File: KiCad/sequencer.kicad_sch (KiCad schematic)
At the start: 35 parts, among them J1 GATE OUT, J2 CLOCK IN, J5 RESET, J6 CV OUT, J7 CLOCK OUT, Q1 BC548, SW10 SW_Nidec_CAS-120A1, U1 TL074

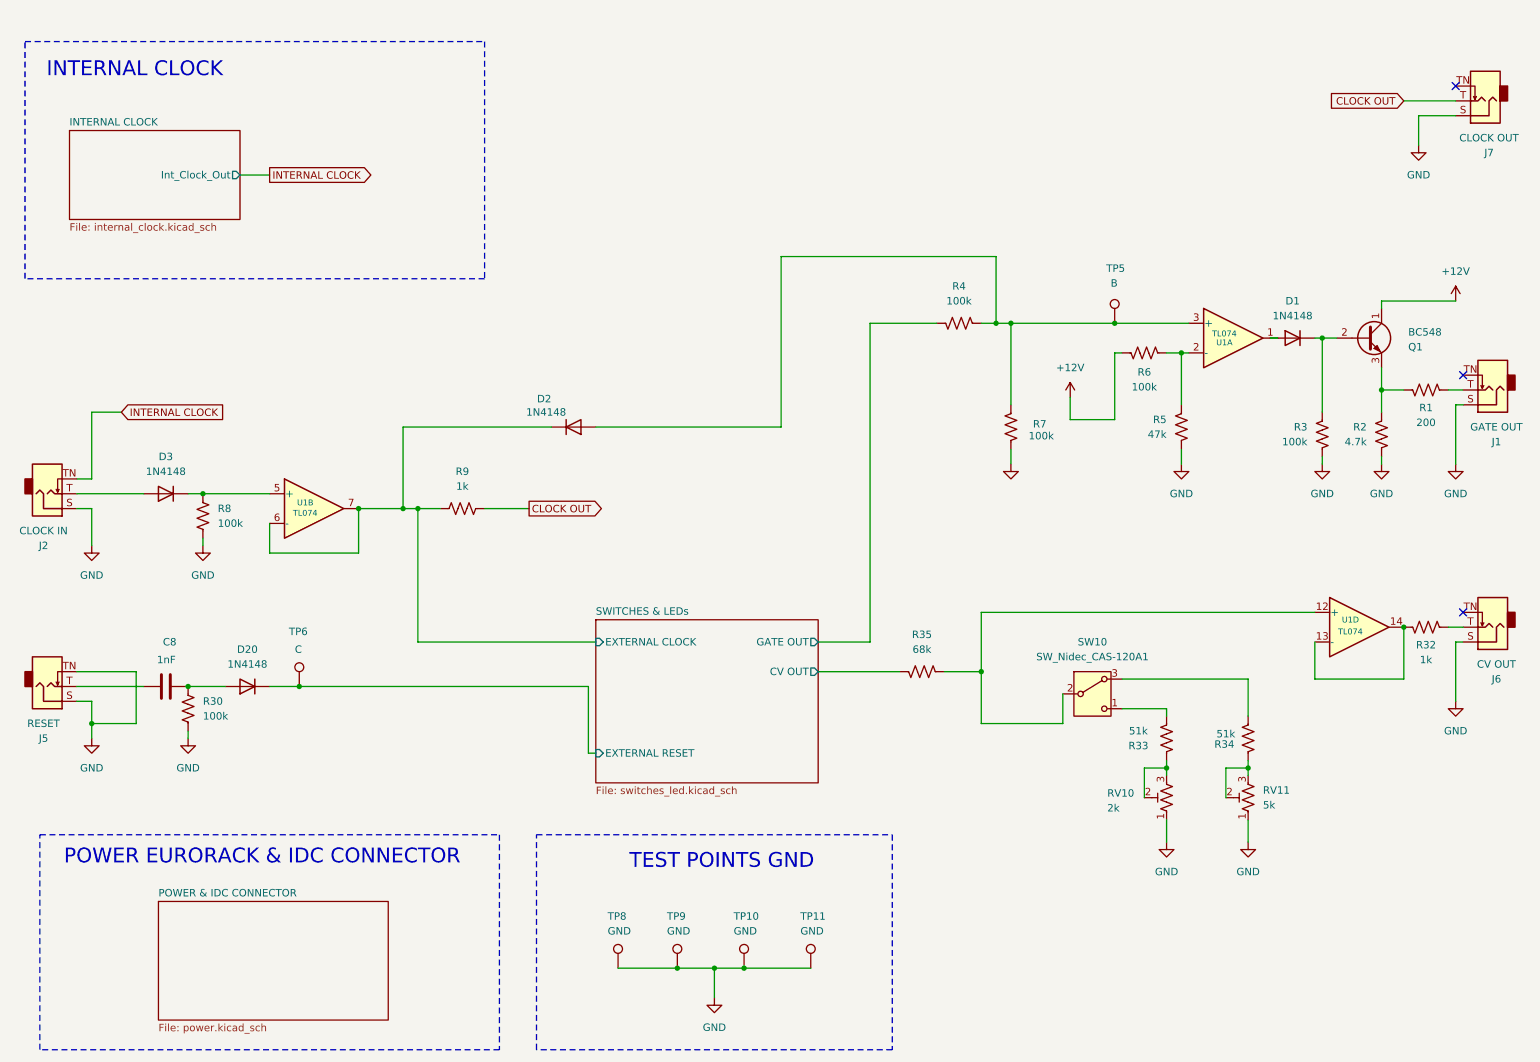
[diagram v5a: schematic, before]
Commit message: Updating sheet names
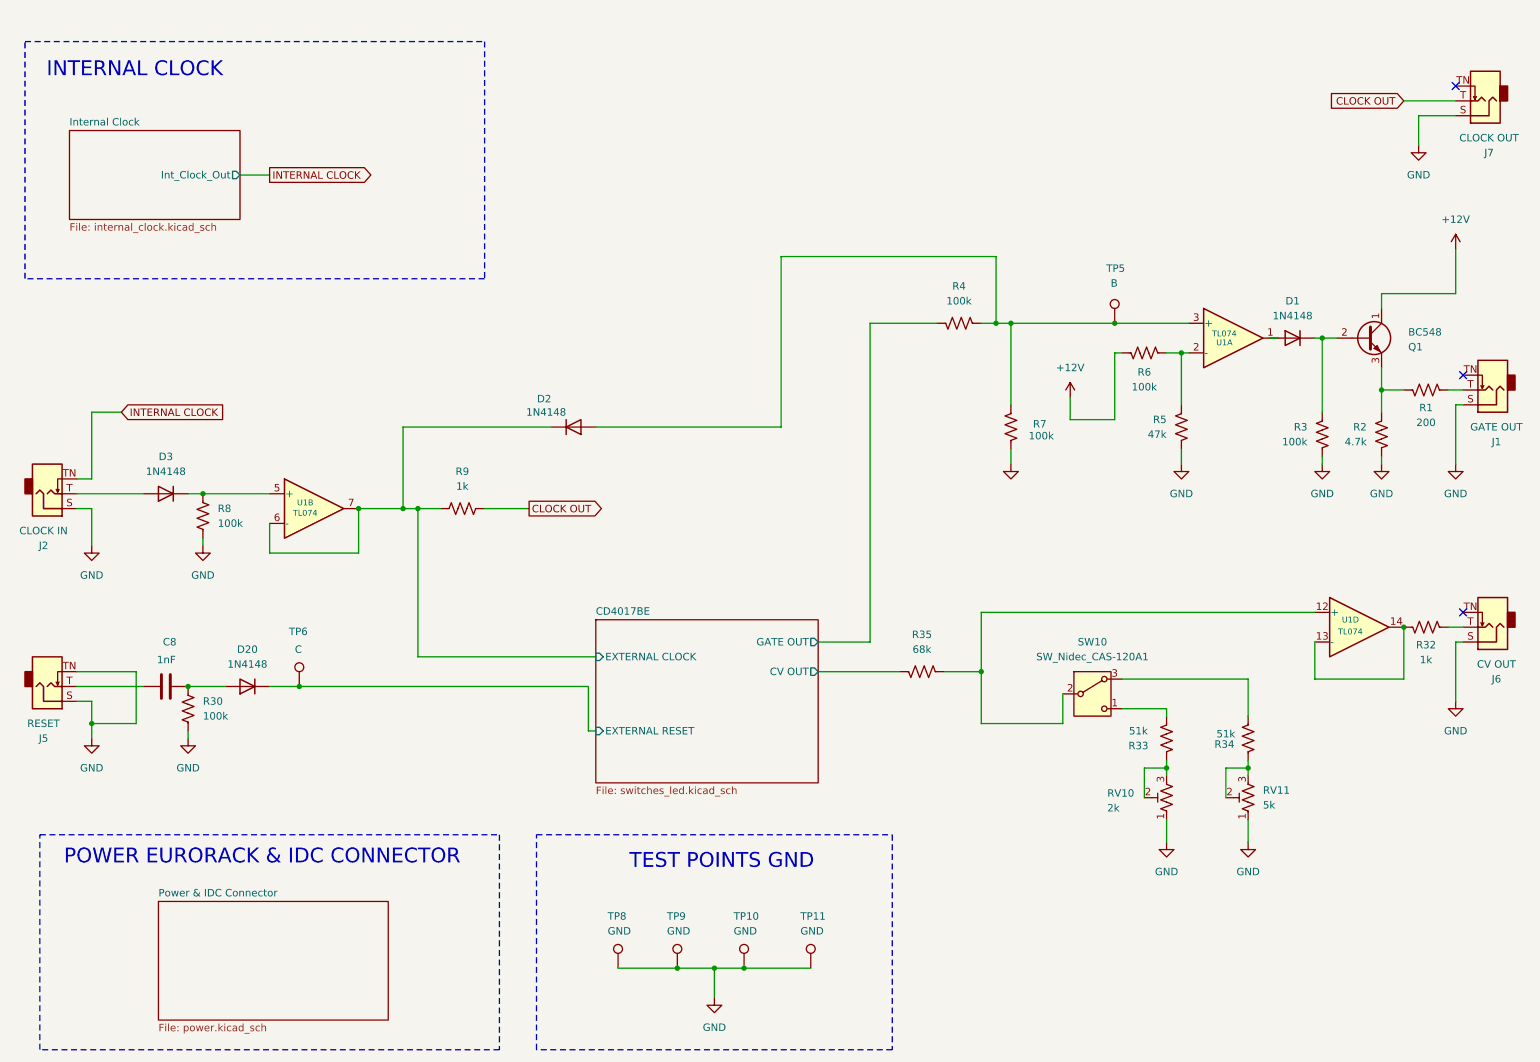
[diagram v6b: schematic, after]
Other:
- sheet INTERNAL CLOCK renamed Internal Clock
- sheet POWER & IDC CONNECTOR renamed Power & IDC Connector
- sheet SWITCHES & LEDs renamed CD4017BE
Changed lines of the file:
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@@
 	(title_block
 		(title "8 Step Sequencer")
-		(date "2026-03-09")
+		(date "2026-03-13")
 		(rev "v0.0")
 		(company "Dirty Dream - Nathanael Noir")
@@
 	(wire
 		(pts
-			(xy 116.84 142.24) (xy 116.84 130.81)
+			(xy 116.84 138.43) (xy 116.84 130.81)
 		)
 		(stroke
@@
 	(wire
 		(pts
-			(xy 252.73 64.77) (xy 265.43 64.77)
+			(xy 252.73 63.5) (xy 265.43 63.5)
 		)
 		(stroke
@@
 	(wire
 		(pts
-			(xy 116.84 142.24) (xy 118.11 142.24)
+			(xy 116.84 138.43) (xy 118.11 138.43)
 		)
 		(stroke
@@
 	(wire
 		(pts
-			(xy 252.73 66.04) (xy 252.73 64.77)
+			(xy 252.73 66.04) (xy 252.73 63.5)
 		)
 		(stroke
@@
 	(wire
 		(pts
-			(xy 87.63 100.33) (xy 87.63 123.19)
+			(xy 87.63 100.33) (xy 87.63 125.73)
 		)
 		(stroke
@@
 	(wire
 		(pts
+			(xy 265.43 55.88) (xy 265.43 63.5)
+		)
+		(stroke
+			(width 0)
+			(type default)
+		)
+	)
+	(wire
+		(pts
 			(xy 265.43 133.35) (xy 265.43 123.19)
 		)
@@
 	(wire
 		(pts
-			(xy 87.63 123.19) (xy 118.11 123.19)
+			(xy 87.63 125.73) (xy 118.11 125.73)
 		)
 		(stroke
@@
 	(symbol
 		(lib_id "power:+12V")
-		(at 265.43 64.77 0)
+		(at 265.43 55.88 0)
 		(mirror y)
 		(unit 1)
@@
 		(fields_autoplaced yes)
 		(property "Reference" "#PWR033"
-			(at 265.43 68.58 0)
+			(at 265.43 59.69 0)
 			(effects
 				(font
@@
 		)
 		(property "Value" "+12V"
-			(at 265.43 59.69 0)
+			(at 265.43 50.8 0)
 			(effects
 				(font
@@
 		)
 		(property "Footprint" ""
-			(at 265.43 64.77 0)
+			(at 265.43 55.88 0)
 			(effects
 				(font
@@
 		)
 		(property "Datasheet" ""
-			(at 265.43 64.77 0)
+			(at 265.43 55.88 0)
 			(effects
 				(font
@@
 		)
 		(property "Description" "Power symbol creates a global label with name \"+12V\""
-			(at 265.43 64.77 0)
+			(at 265.43 55.88 0)
 			(effects
 				(font
@@
 			(color 0 0 0 0.0000)
 		)
-		(property "Sheetname" "POWER & IDC CONNECTOR"
+		(property "Sheetname" "Power & IDC Connector"
 			(at 43.18 166.9284 0)
 			(effects
@@
 			(color 0 0 0 0.0000)
 		)
-		(property "Sheetname" "SWITCHES & LEDs"
+		(property "Sheetname" "CD4017BE"
 			(at 118.11 118.6684 0)
 			(effects
@@
 		)
 		(pin "EXTERNAL CLOCK" input
-			(at 118.11 123.19 180)
+			(at 118.11 125.73 180)
 			(effects
 				(font
@@
 		)
 		(pin "EXTERNAL RESET" input
-			(at 118.11 142.24 180)
+			(at 118.11 138.43 180)
 			(effects
 				(font
@@
 			(color 0 0 0 0.0000)
 		)
-		(property "Sheetname" "INTERNAL CLOCK"
+		(property "Sheetname" "Internal Clock"
 			(at 27.94 34.8484 0)
 			(effects

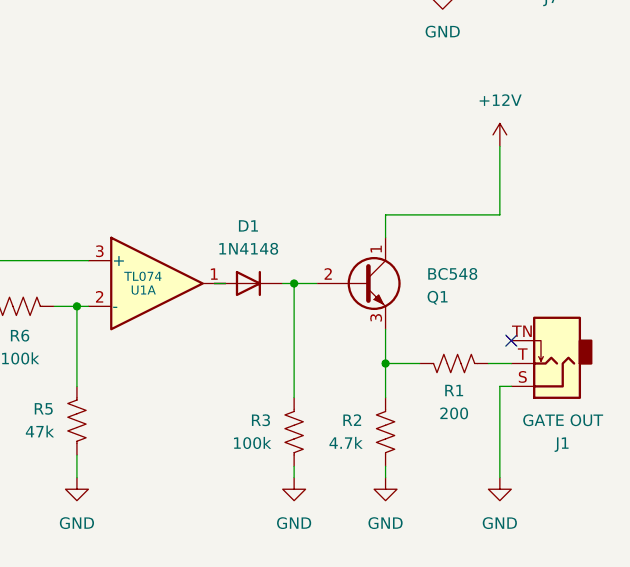
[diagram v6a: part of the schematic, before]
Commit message: adding missing SMD footprints
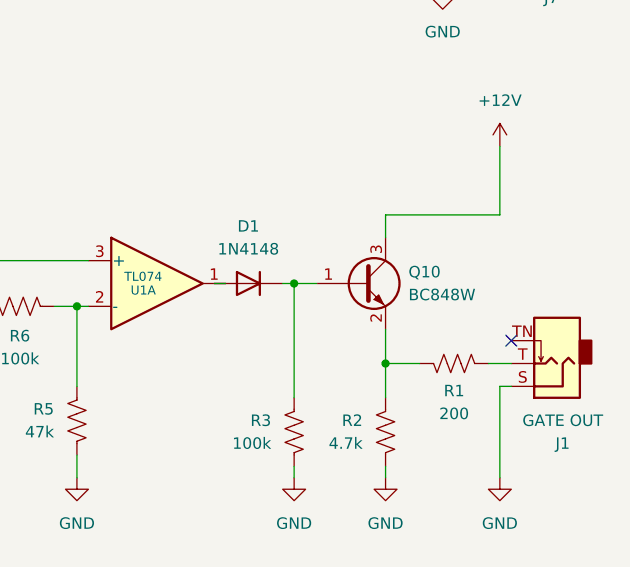
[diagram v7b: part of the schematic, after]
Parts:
- removed Q1: BC548, Package_TO_SOT_THT:TO-92_Inline, symbol Transistor_BJT:BC548
- added Q10: BC848W, Package_TO_SOT_SMD:SOT-323_SC-70, symbol Transistor_BJT:BC848W
- D1, D2, D20, D3: footprint Diode_THT:D_DO-35_SOD27_P7.62mm_Horizontal -> Diode_SMD:D_SOD-323_HandSoldering
- J1, J2, J5, J6, J7: footprint (none) -> Eurorack:Jack_3.5mm_QingPu_WQP-PJ398SM_Vertical
- R1, R2, R3, R30, R32, R33, R34, R35, R4, R5, R6, R7, R8, R9: footprint (none) -> Resistor_SMD:R_0805_2012Metric_Pad1.20x1.40mm_HandSolder
- TP10, TP11, TP5, TP6, TP8, TP9: footprint (none) -> TestPoint:TestPoint_Pad_D1.5mm
- U1: footprint (none) -> Package_SO:SOIC-14_3.9x8.7mm_P1.27mm
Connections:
- net +12V: now also Q10.3 (C)
- net at R1.2, R2.2: now also Q10.2 (E)
- net at D1.1 (K), R3.2: now also Q10.1 (B)

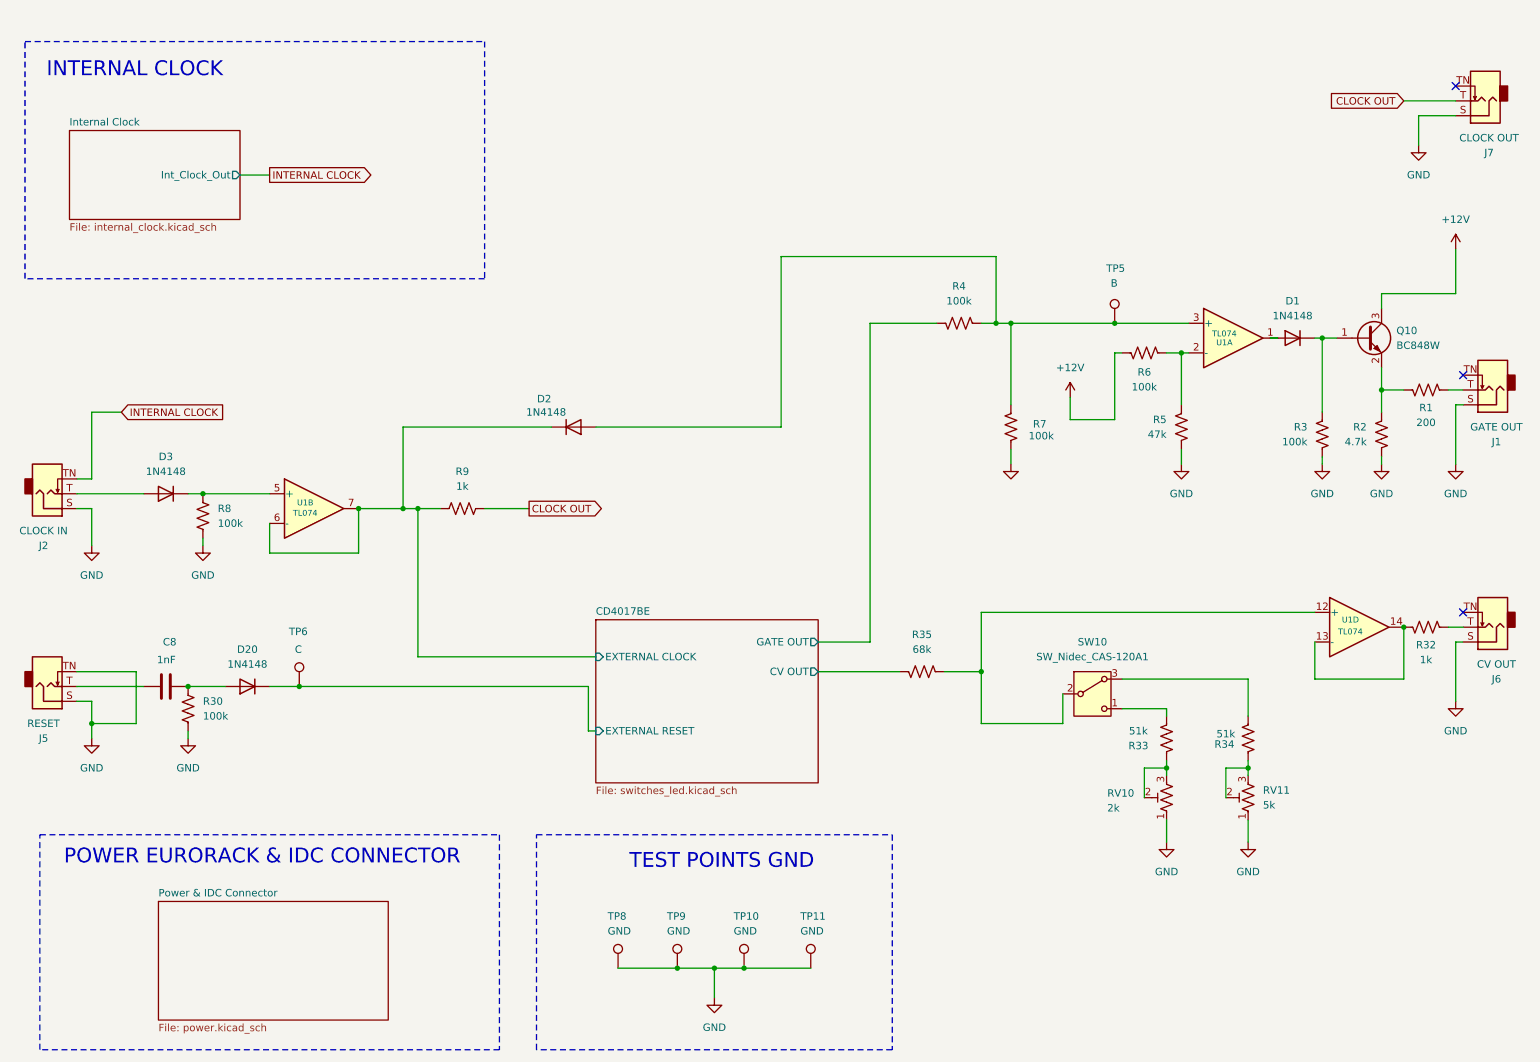
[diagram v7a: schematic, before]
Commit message: adding Test Point D
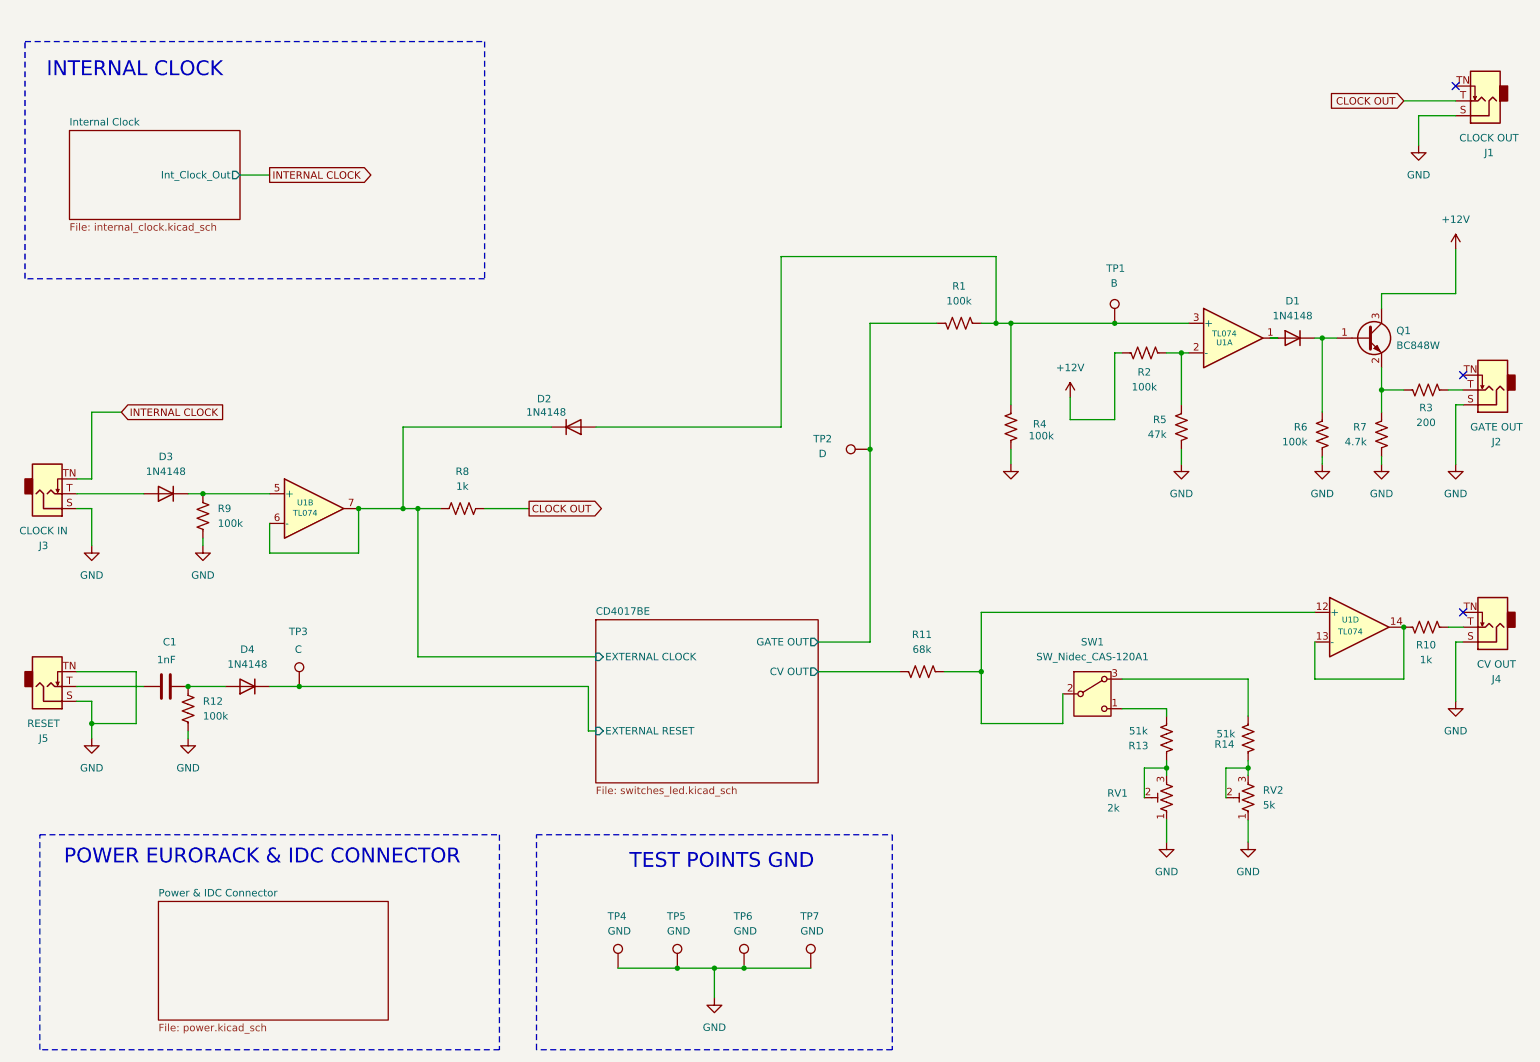
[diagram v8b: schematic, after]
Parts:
- added TP2: D, TestPoint:TestPoint_Pad_D1.5mm, symbol Connector:TestPoint
- renumbered C8 to C1, D20 to D4, J7 to J1, J1 to J2, J2 to J3, J6 to J4, Q10 to Q1, R4 to R1, R32 to R10, R35 to R11, R30 to R12, R33 to R13, R34 to R14, R6 to R2, R1 to R3, R7 to R4, R3 to R6, R2 to R7, R9 to R8, R8 to R9, RV10 to RV1, RV11 to RV2, SW10 to SW1, TP5 to TP1, TP6 to TP3, TP8 to TP4, TP9 to TP5, TP10 to TP6, TP11 to TP7
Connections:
- net CD4017BE/GATE OUT: now also TP2.1
